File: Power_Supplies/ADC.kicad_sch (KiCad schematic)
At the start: 28 parts, among them IC1 PCM1865DBT, IC5 PCM1865DBT

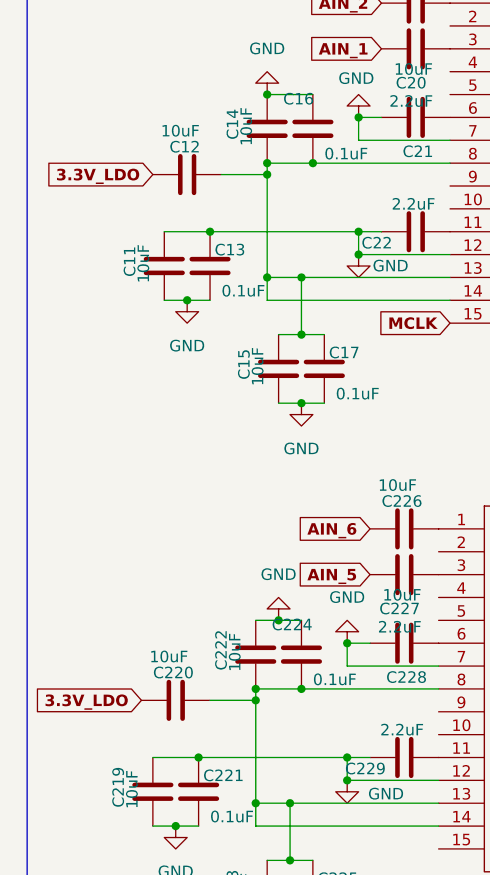
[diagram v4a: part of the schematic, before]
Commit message: Add files via upload
fixed voltage issues
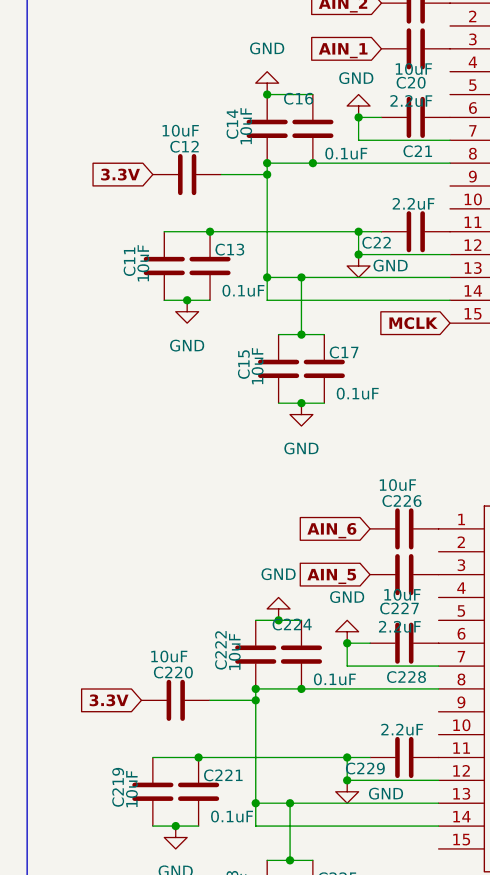
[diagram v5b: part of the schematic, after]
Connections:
- net 3.3V_LDO renamed 3.3V
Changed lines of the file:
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@@
 		)
 	)
-	(global_label "3.3V_LDO"
+	(global_label "3.3V"
 		(shape input)
 		(at 31.75 124.46 180)
@@
 		)
 		(property "Intersheetrefs" "${INTERSHEET_REFS}"
-			(at 19.5802 124.46 0)
+			(at 24.1764 124.46 0)
 			(effects
 				(font
@@
 		)
 	)
-	(global_label "3.3V_LDO"
+	(global_label "3.3V"
 		(shape input)
 		(at 33.02 66.04 180)
@@
 		)
 		(property "Intersheetrefs" "${INTERSHEET_REFS}"
-			(at 20.8502 66.04 0)
+			(at 25.4464 66.04 0)
 			(effects
 				(font
@@
 		(exclude_from_sim no)
 		(in_bom yes)
-		(on_board no)
+		(on_board yes)
 		(dnp no)
 		(property "Reference" "C16"
@@
 		(exclude_from_sim no)
 		(in_bom yes)
-		(on_board no)
+		(on_board yes)
 		(dnp no)
 		(property "Reference" "C220"
@@
 		(exclude_from_sim no)
 		(in_bom yes)
-		(on_board no)
+		(on_board yes)
 		(dnp no)
 		(property "Reference" "C225"
@@
 		(exclude_from_sim no)
 		(in_bom yes)
-		(on_board no)
+		(on_board yes)
 		(dnp no)
 		(property "Reference" "C221"
@@
 		(exclude_from_sim no)
 		(in_bom yes)
-		(on_board no)
+		(on_board yes)
 		(dnp no)
 		(property "Reference" "C22"
@@
 		(exclude_from_sim no)
 		(in_bom yes)
-		(on_board no)
+		(on_board yes)
 		(dnp no)
 		(fields_autoplaced yes)
@@
 		(exclude_from_sim no)
 		(in_bom yes)
-		(on_board no)
+		(on_board yes)
 		(dnp no)
 		(property "Reference" "#PWR028"
@@
 		(exclude_from_sim no)
 		(in_bom yes)
-		(on_board no)
+		(on_board yes)
 		(dnp no)
 		(property "Reference" "C229"
@@
 		(exclude_from_sim no)
 		(in_bom yes)
-		(on_board no)
+		(on_board yes)
 		(dnp no)
 		(property "Reference" "#PWR0216"
@@
 		(exclude_from_sim no)
 		(in_bom yes)
-		(on_board no)
+		(on_board yes)
 		(dnp no)
 		(fields_autoplaced yes)
@@
 		(exclude_from_sim no)
 		(in_bom yes)
-		(on_board no)
+		(on_board yes)
 		(dnp no)
 		(property "Reference" "C231"
@@
 		(exclude_from_sim no)
 		(in_bom yes)
-		(on_board no)
+		(on_board yes)
 		(dnp no)
 		(fields_autoplaced yes)
@@
 		(exclude_from_sim no)
 		(in_bom yes)
-		(on_board no)
+		(on_board yes)
 		(dnp no)
 		(property "Reference" "C227"
@@
 		(exclude_from_sim no)
 		(in_bom yes)
-		(on_board no)
+		(on_board yes)
 		(dnp no)
 		(property "Reference" "C14"
@@
 		(exclude_from_sim no)
 		(in_bom yes)
-		(on_board no)
+		(on_board yes)
 		(dnp no)
 		(fields_autoplaced yes)
@@
 		(exclude_from_sim no)
 		(in_bom yes)
-		(on_board no)
+		(on_board yes)
 		(dnp no)
 		(fields_autoplaced yes)
@@
 		(exclude_from_sim no)
 		(in_bom yes)
-		(on_board no)
+		(on_board yes)
 		(dnp no)
 		(property "Reference" "C11"
@@
 		(exclude_from_sim no)
 		(in_bom yes)
-		(on_board no)
+		(on_board yes)
 		(dnp no)
 		(property "Reference" "C21"
@@
 		(exclude_from_sim no)
 		(in_bom yes)
-		(on_board no)
+		(on_board yes)
 		(dnp no)
 		(property "Reference" "C15"
@@
 		(exclude_from_sim no)
 		(in_bom yes)
-		(on_board no)
+		(on_board yes)
 		(dnp no)
 		(property "Reference" "C223"
@@
 		(exclude_from_sim no)
 		(in_bom yes)
-		(on_board no)
+		(on_board yes)
 		(dnp no)
 		(property "Reference" "C19"
@@
 		(exclude_from_sim no)
 		(in_bom yes)
-		(on_board no)
+		(on_board yes)
 		(dnp no)
 		(property "Reference" "C219"
@@
 		(exclude_from_sim no)
 		(in_bom yes)
-		(on_board no)
+		(on_board yes)
 		(dnp no)
 		(fields_autoplaced yes)
@@
 		(exclude_from_sim no)
 		(in_bom yes)
-		(on_board no)
+		(on_board yes)
 		(dnp no)
 		(fields_autoplaced yes)
@@
 		(exclude_from_sim no)
 		(in_bom yes)
-		(on_board no)
+		(on_board yes)
 		(dnp no)
 		(property "Reference" "C228"
@@
 		(exclude_from_sim no)
 		(in_bom yes)
-		(on_board no)
+		(on_board yes)
 		(dnp no)
 		(property "Reference" "C226"
@@
 		(exclude_from_sim no)
 		(in_bom yes)
-		(on_board no)
+		(on_board yes)
 		(dnp no)
 		(fields_autoplaced yes)
@@
 		(exclude_from_sim no)
 		(in_bom yes)
-		(on_board no)
+		(on_board yes)
 		(dnp no)
 		(property "Reference" "C230"
@@
 		(exclude_from_sim no)
 		(in_bom yes)
-		(on_board no)
+		(on_board yes)
 		(dnp no)
 		(fields_autoplaced yes)
@@
 		(exclude_from_sim no)
 		(in_bom yes)
-		(on_board no)
+		(on_board yes)
 		(dnp no)
 		(property "Reference" "C224"
@@
 		(exclude_from_sim no)
 		(in_bom yes)
-		(on_board no)
+		(on_board yes)
 		(dnp no)
 		(property "Reference" "#PWR029"
@@
 		(exclude_from_sim no)
 		(in_bom yes)
-		(on_board no)
+		(on_board yes)
 		(dnp no)
 		(fields_autoplaced yes)
@@
 		(exclude_from_sim no)
 		(in_bom yes)
-		(on_board no)
+		(on_board yes)
 		(dnp no)
 		(property "Reference" "C17"
@@
 		(exclude_from_sim no)
 		(in_bom yes)
-		(on_board no)
+		(on_board yes)
 		(dnp no)
 		(property "Reference" "C27"
@@
 		(exclude_from_sim no)
 		(in_bom yes)
-		(on_board no)
+		(on_board yes)
 		(dnp no)
 		(property "Reference" "C28"
@@
 		(exclude_from_sim no)
 		(in_bom yes)
-		(on_board no)
+		(on_board yes)
 		(dnp no)
 		(property "Reference" "C222"
@@
 		(exclude_from_sim no)
 		(in_bom yes)
-		(on_board no)
+		(on_board yes)
 		(dnp no)
 		(property "Reference" "C20"
@@
 		(exclude_from_sim no)
 		(in_bom yes)
-		(on_board no)
+		(on_board yes)
 		(dnp no)
 		(fields_autoplaced yes)
@@
 		(exclude_from_sim no)
 		(in_bom yes)
-		(on_board no)
+		(on_board yes)
 		(dnp no)
 		(property "Reference" "C13"
@@
 		(exclude_from_sim no)
 		(in_bom yes)
-		(on_board no)
+		(on_board yes)
 		(dnp no)
 		(property "Reference" "C12"

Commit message: connected ADC/DACs, USB
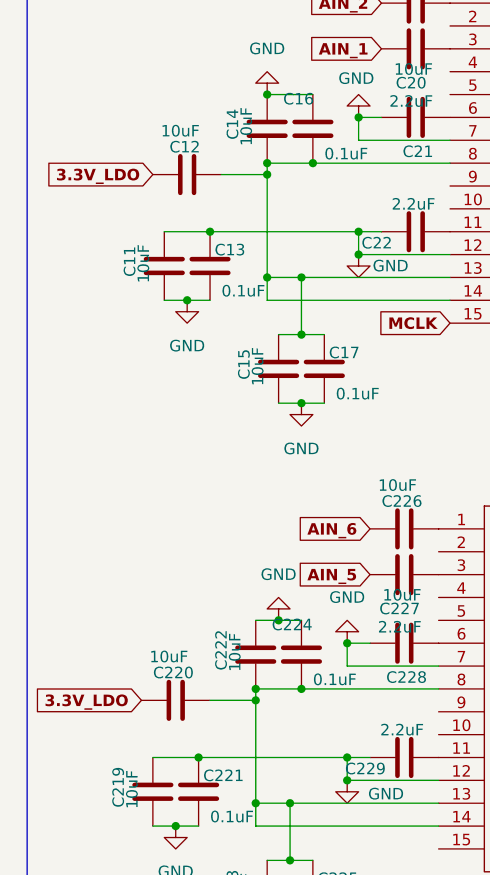
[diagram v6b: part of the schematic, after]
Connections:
- net 3.3V renamed 3.3V_LDO
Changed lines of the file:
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@@
 		)
 	)
-	(global_label "3.3V"
+	(global_label "3.3V_LDO"
 		(shape input)
 		(at 31.75 124.46 180)
@@
 		)
 		(property "Intersheetrefs" "${INTERSHEET_REFS}"
-			(at 24.1764 124.46 0)
+			(at 19.5802 124.46 0)
 			(effects
 				(font
@@
 		)
 	)
-	(global_label "3.3V"
+	(global_label "3.3V_LDO"
 		(shape input)
 		(at 33.02 66.04 180)
@@
 		)
 		(property "Intersheetrefs" "${INTERSHEET_REFS}"
-			(at 25.4464 66.04 0)
+			(at 20.8502 66.04 0)
 			(effects
 				(font
@@
 		(exclude_from_sim no)
 		(in_bom yes)
-		(on_board yes)
+		(on_board no)
 		(dnp no)
 		(property "Reference" "C16"
@@
 		(exclude_from_sim no)
 		(in_bom yes)
-		(on_board yes)
+		(on_board no)
 		(dnp no)
 		(property "Reference" "C220"
@@
 		(exclude_from_sim no)
 		(in_bom yes)
-		(on_board yes)
+		(on_board no)
 		(dnp no)
 		(property "Reference" "C225"
@@
 		(exclude_from_sim no)
 		(in_bom yes)
-		(on_board yes)
+		(on_board no)
 		(dnp no)
 		(property "Reference" "C221"
@@
 		(exclude_from_sim no)
 		(in_bom yes)
-		(on_board yes)
+		(on_board no)
 		(dnp no)
 		(property "Reference" "C22"
@@
 		(exclude_from_sim no)
 		(in_bom yes)
-		(on_board yes)
+		(on_board no)
 		(dnp no)
 		(fields_autoplaced yes)
@@
 		(exclude_from_sim no)
 		(in_bom yes)
-		(on_board yes)
+		(on_board no)
 		(dnp no)
 		(property "Reference" "#PWR028"
@@
 		(exclude_from_sim no)
 		(in_bom yes)
-		(on_board yes)
+		(on_board no)
 		(dnp no)
 		(property "Reference" "C229"
@@
 		(exclude_from_sim no)
 		(in_bom yes)
-		(on_board yes)
+		(on_board no)
 		(dnp no)
 		(property "Reference" "#PWR0216"
@@
 		(exclude_from_sim no)
 		(in_bom yes)
-		(on_board yes)
+		(on_board no)
 		(dnp no)
 		(fields_autoplaced yes)
@@
 		(exclude_from_sim no)
 		(in_bom yes)
-		(on_board yes)
+		(on_board no)
 		(dnp no)
 		(property "Reference" "C231"
@@
 		(exclude_from_sim no)
 		(in_bom yes)
-		(on_board yes)
+		(on_board no)
 		(dnp no)
 		(fields_autoplaced yes)
@@
 		(exclude_from_sim no)
 		(in_bom yes)
-		(on_board yes)
+		(on_board no)
 		(dnp no)
 		(property "Reference" "C227"
@@
 		(exclude_from_sim no)
 		(in_bom yes)
-		(on_board yes)
+		(on_board no)
 		(dnp no)
 		(property "Reference" "C14"
@@
 		(exclude_from_sim no)
 		(in_bom yes)
-		(on_board yes)
+		(on_board no)
 		(dnp no)
 		(fields_autoplaced yes)
@@
 		(exclude_from_sim no)
 		(in_bom yes)
-		(on_board yes)
+		(on_board no)
 		(dnp no)
 		(fields_autoplaced yes)
@@
 		(exclude_from_sim no)
 		(in_bom yes)
-		(on_board yes)
+		(on_board no)
 		(dnp no)
 		(property "Reference" "C11"
@@
 		(exclude_from_sim no)
 		(in_bom yes)
-		(on_board yes)
+		(on_board no)
 		(dnp no)
 		(property "Reference" "C21"
@@
 		(exclude_from_sim no)
 		(in_bom yes)
-		(on_board yes)
+		(on_board no)
 		(dnp no)
 		(property "Reference" "C15"
@@
 		(exclude_from_sim no)
 		(in_bom yes)
-		(on_board yes)
+		(on_board no)
 		(dnp no)
 		(property "Reference" "C223"
@@
 		(exclude_from_sim no)
 		(in_bom yes)
-		(on_board yes)
+		(on_board no)
 		(dnp no)
 		(property "Reference" "C19"
@@
 		(exclude_from_sim no)
 		(in_bom yes)
-		(on_board yes)
+		(on_board no)
 		(dnp no)
 		(property "Reference" "C219"
@@
 		(exclude_from_sim no)
 		(in_bom yes)
-		(on_board yes)
+		(on_board no)
 		(dnp no)
 		(fields_autoplaced yes)
@@
 		(exclude_from_sim no)
 		(in_bom yes)
-		(on_board yes)
+		(on_board no)
 		(dnp no)
 		(fields_autoplaced yes)
@@
 		(exclude_from_sim no)
 		(in_bom yes)
-		(on_board yes)
+		(on_board no)
 		(dnp no)
 		(property "Reference" "C228"
@@
 		(exclude_from_sim no)
 		(in_bom yes)
-		(on_board yes)
+		(on_board no)
 		(dnp no)
 		(property "Reference" "C226"
@@
 		(exclude_from_sim no)
 		(in_bom yes)
-		(on_board yes)
+		(on_board no)
 		(dnp no)
 		(fields_autoplaced yes)
@@
 		(exclude_from_sim no)
 		(in_bom yes)
-		(on_board yes)
+		(on_board no)
 		(dnp no)
 		(property "Reference" "C230"
@@
 		(exclude_from_sim no)
 		(in_bom yes)
-		(on_board yes)
+		(on_board no)
 		(dnp no)
 		(fields_autoplaced yes)
@@
 		(exclude_from_sim no)
 		(in_bom yes)
-		(on_board yes)
+		(on_board no)
 		(dnp no)
 		(property "Reference" "C224"
@@
 		(exclude_from_sim no)
 		(in_bom yes)
-		(on_board yes)
+		(on_board no)
 		(dnp no)
 		(property "Reference" "#PWR029"
@@
 		(exclude_from_sim no)
 		(in_bom yes)
-		(on_board yes)
+		(on_board no)
 		(dnp no)
 		(fields_autoplaced yes)
@@
 		(exclude_from_sim no)
 		(in_bom yes)
-		(on_board yes)
+		(on_board no)
 		(dnp no)
 		(property "Reference" "C17"
@@
 		(exclude_from_sim no)
 		(in_bom yes)
-		(on_board yes)
+		(on_board no)
 		(dnp no)
 		(property "Reference" "C27"
@@
 		(exclude_from_sim no)
 		(in_bom yes)
-		(on_board yes)
+		(on_board no)
 		(dnp no)
 		(property "Reference" "C28"
@@
 		(exclude_from_sim no)
 		(in_bom yes)
-		(on_board yes)
+		(on_board no)
 		(dnp no)
 		(property "Reference" "C222"
@@
 		(exclude_from_sim no)
 		(in_bom yes)
-		(on_board yes)
+		(on_board no)
 		(dnp no)
 		(property "Reference" "C20"
@@
 		(exclude_from_sim no)
 		(in_bom yes)
-		(on_board yes)
+		(on_board no)
 		(dnp no)
 		(fields_autoplaced yes)
@@
 		(exclude_from_sim no)
 		(in_bom yes)
-		(on_board yes)
+		(on_board no)
 		(dnp no)
 		(property "Reference" "C13"
@@
 		(exclude_from_sim no)
 		(in_bom yes)
-		(on_board yes)
+		(on_board no)
 		(dnp no)
 		(property "Reference" "C12"

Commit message: Add files via upload
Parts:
- added R42: 5k, Resistor_SMD:R_0402_1005Metric_Pad0.72x0.64mm_HandSolder, symbol Device:R
- C13, C16, C17, C221, C224, C225: footprint Capacitor_SMD:C_0805_2012Metric -> Capacitor_SMD:C_0603_1608Metric_Pad1.08x0.95mm_HandSolder
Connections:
- net GND: now also IC1.25 (MS/AD)
- net 3.3V_LDO renamed 3.3V
- net 3.3V: now also R42.2
- net ADDRESS: no longer names the net of IC5.25 (MS/AD)
- net ADDRESS: now also R42.1; no longer IC1.25 (MS/AD)
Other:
- note added: "Grounded = 0x94"
- note added: "On = 0x96"
